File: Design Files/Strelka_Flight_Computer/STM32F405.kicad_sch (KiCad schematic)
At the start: 21 parts

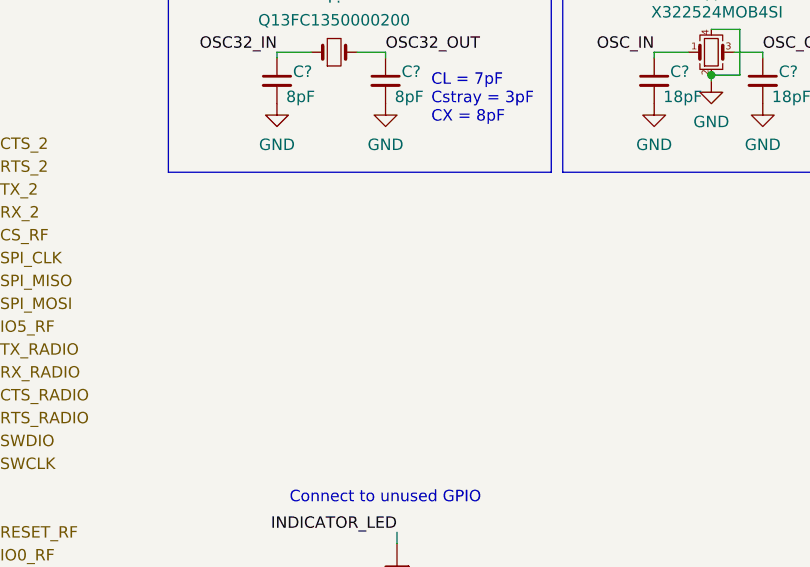
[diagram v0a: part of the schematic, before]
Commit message: Added BMX055
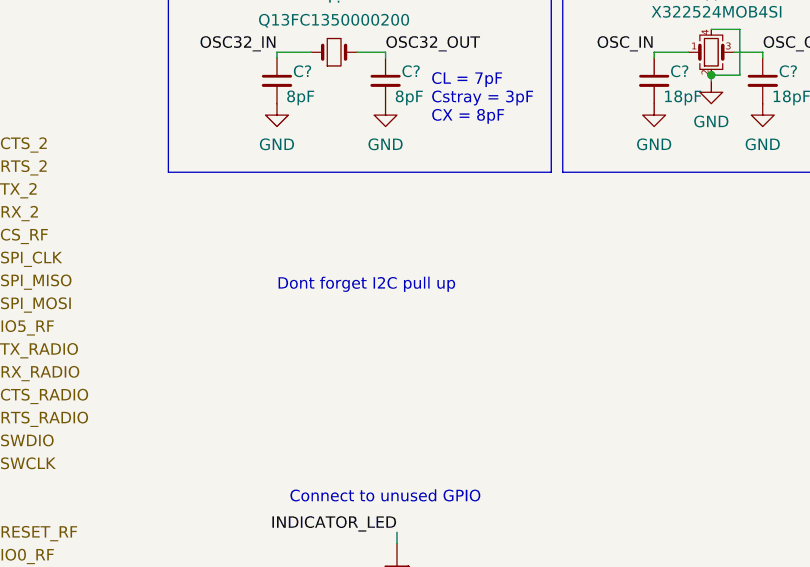
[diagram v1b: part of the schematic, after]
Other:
- note added: "Dont forget I2C pull up"
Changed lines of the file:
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@@
+    (effects (font (size 1.27 1.27)) (justify left bottom))
+  )
+  (text "Dont forget I2C pull up" (at 191.77 83.82 0)
     (effects (font (size 1.27 1.27)) (justify left bottom))
   )

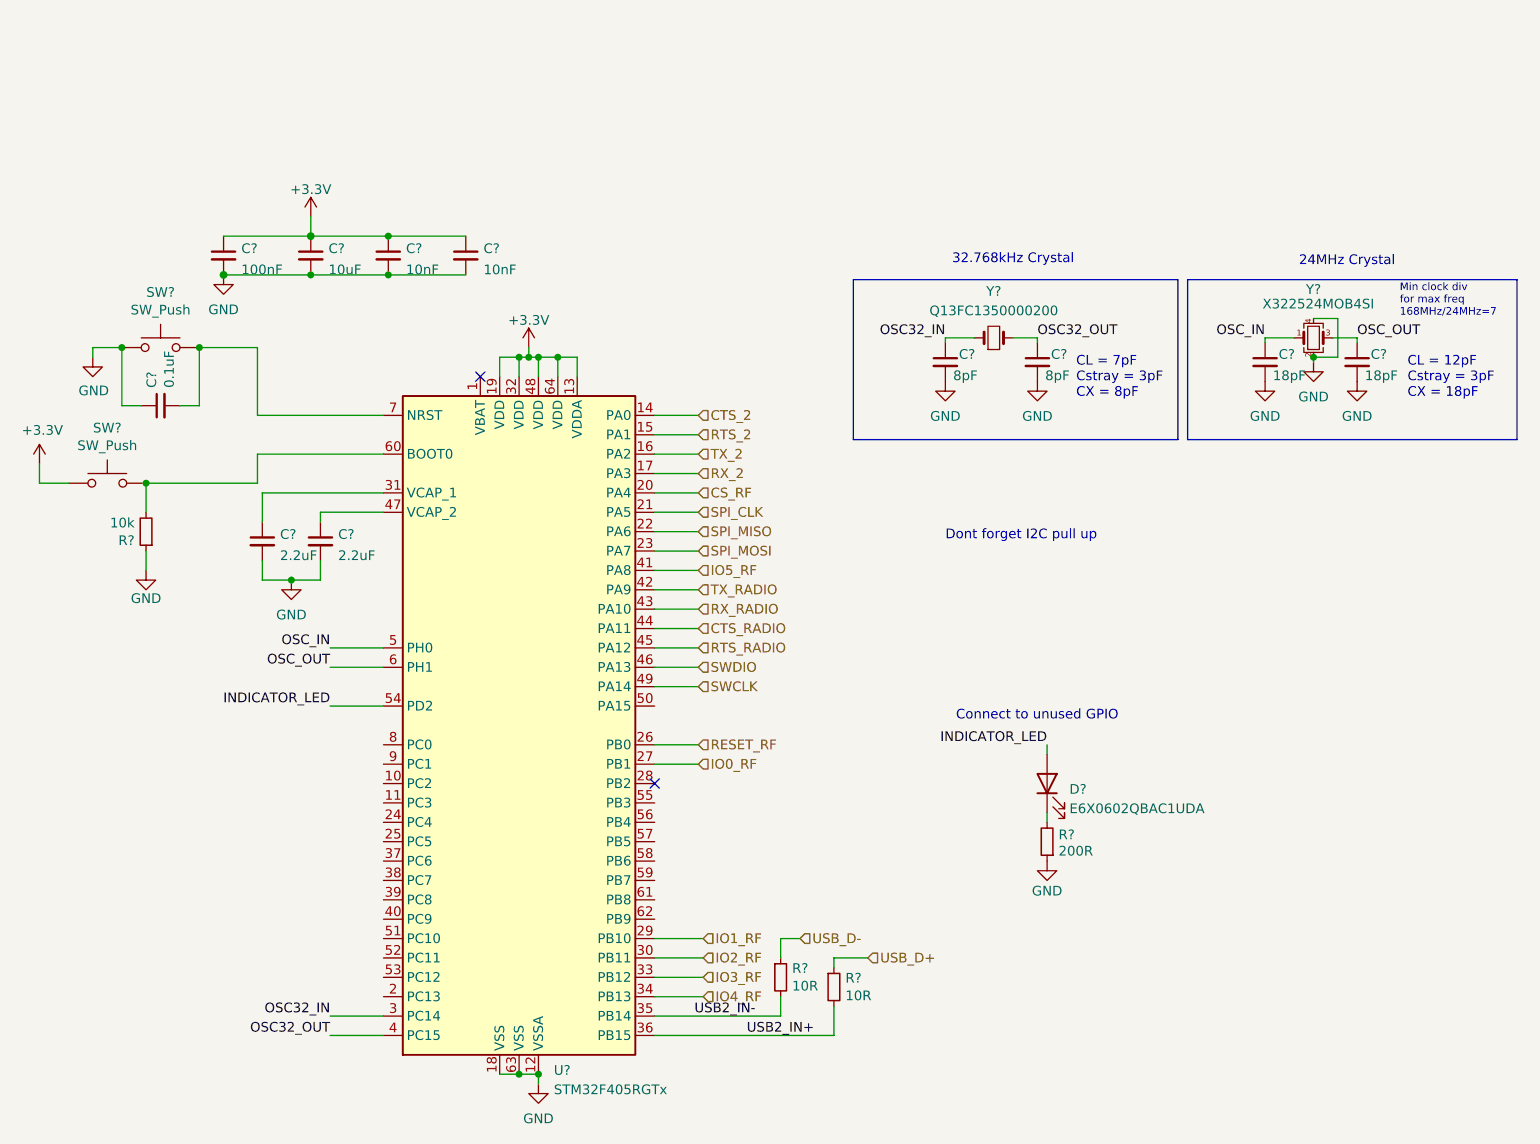
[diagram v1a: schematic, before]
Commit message: Working SPICE sim for ematch continuity circuit
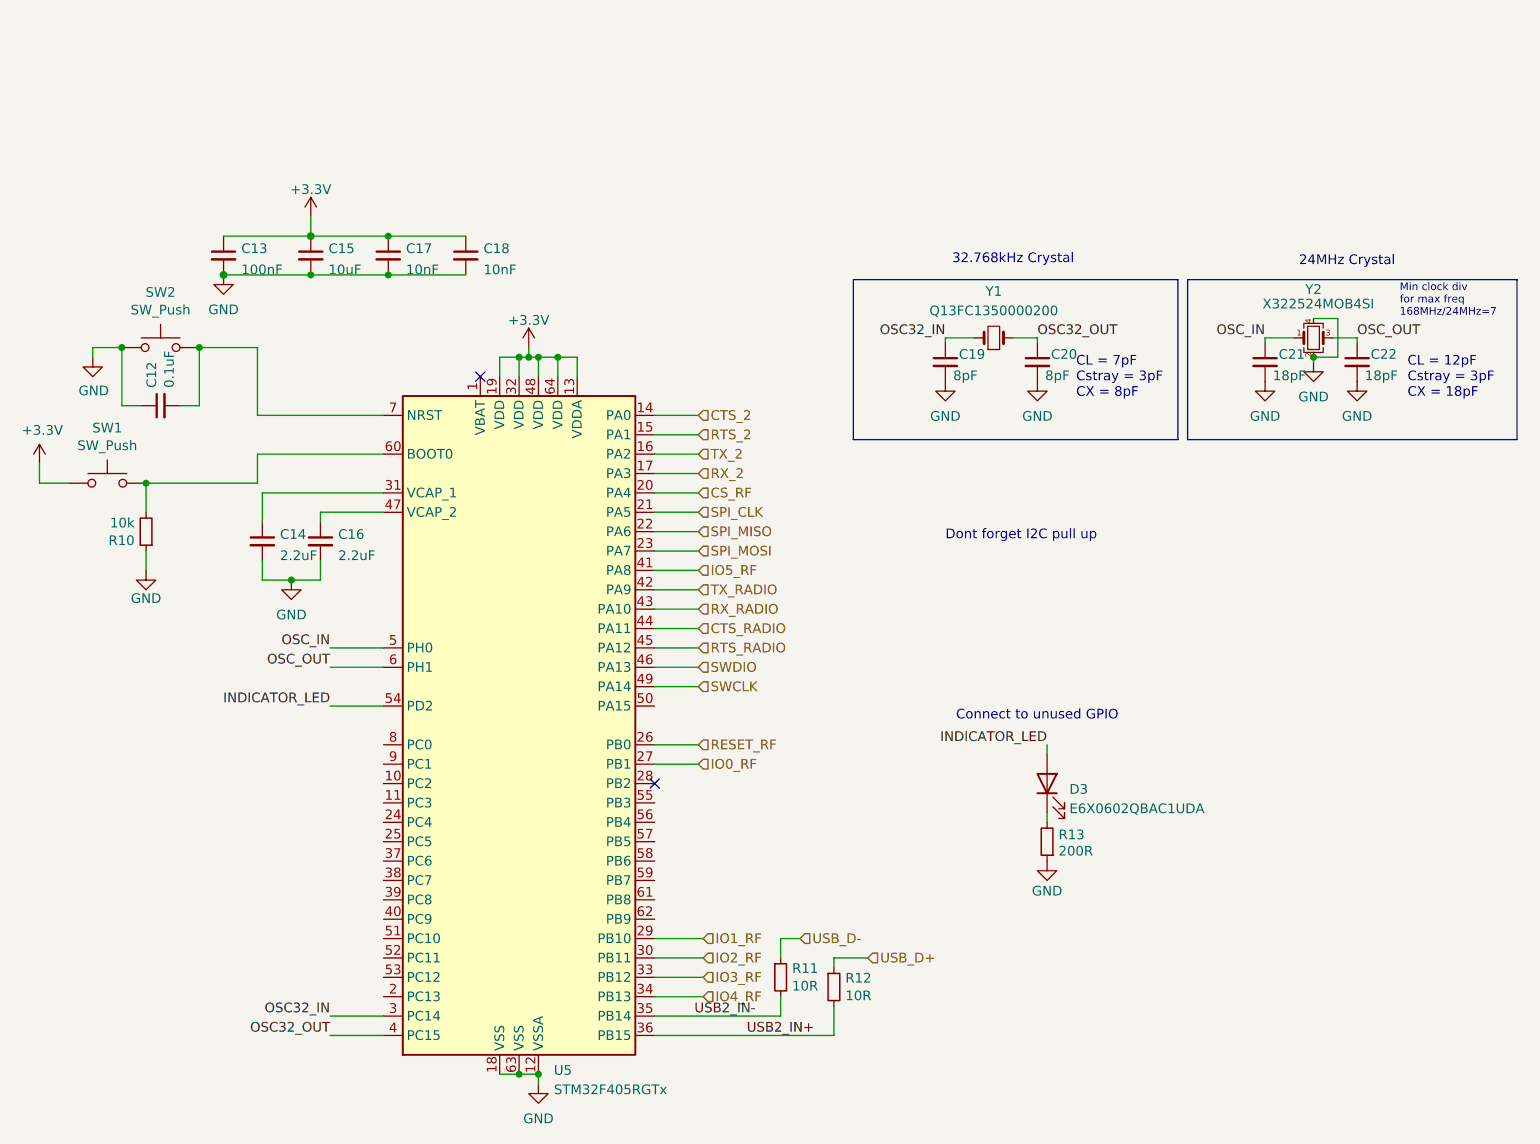
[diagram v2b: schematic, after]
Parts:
- gave numbers to parts that had none: 21

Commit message: Added power board, almost finished Strelka schematic
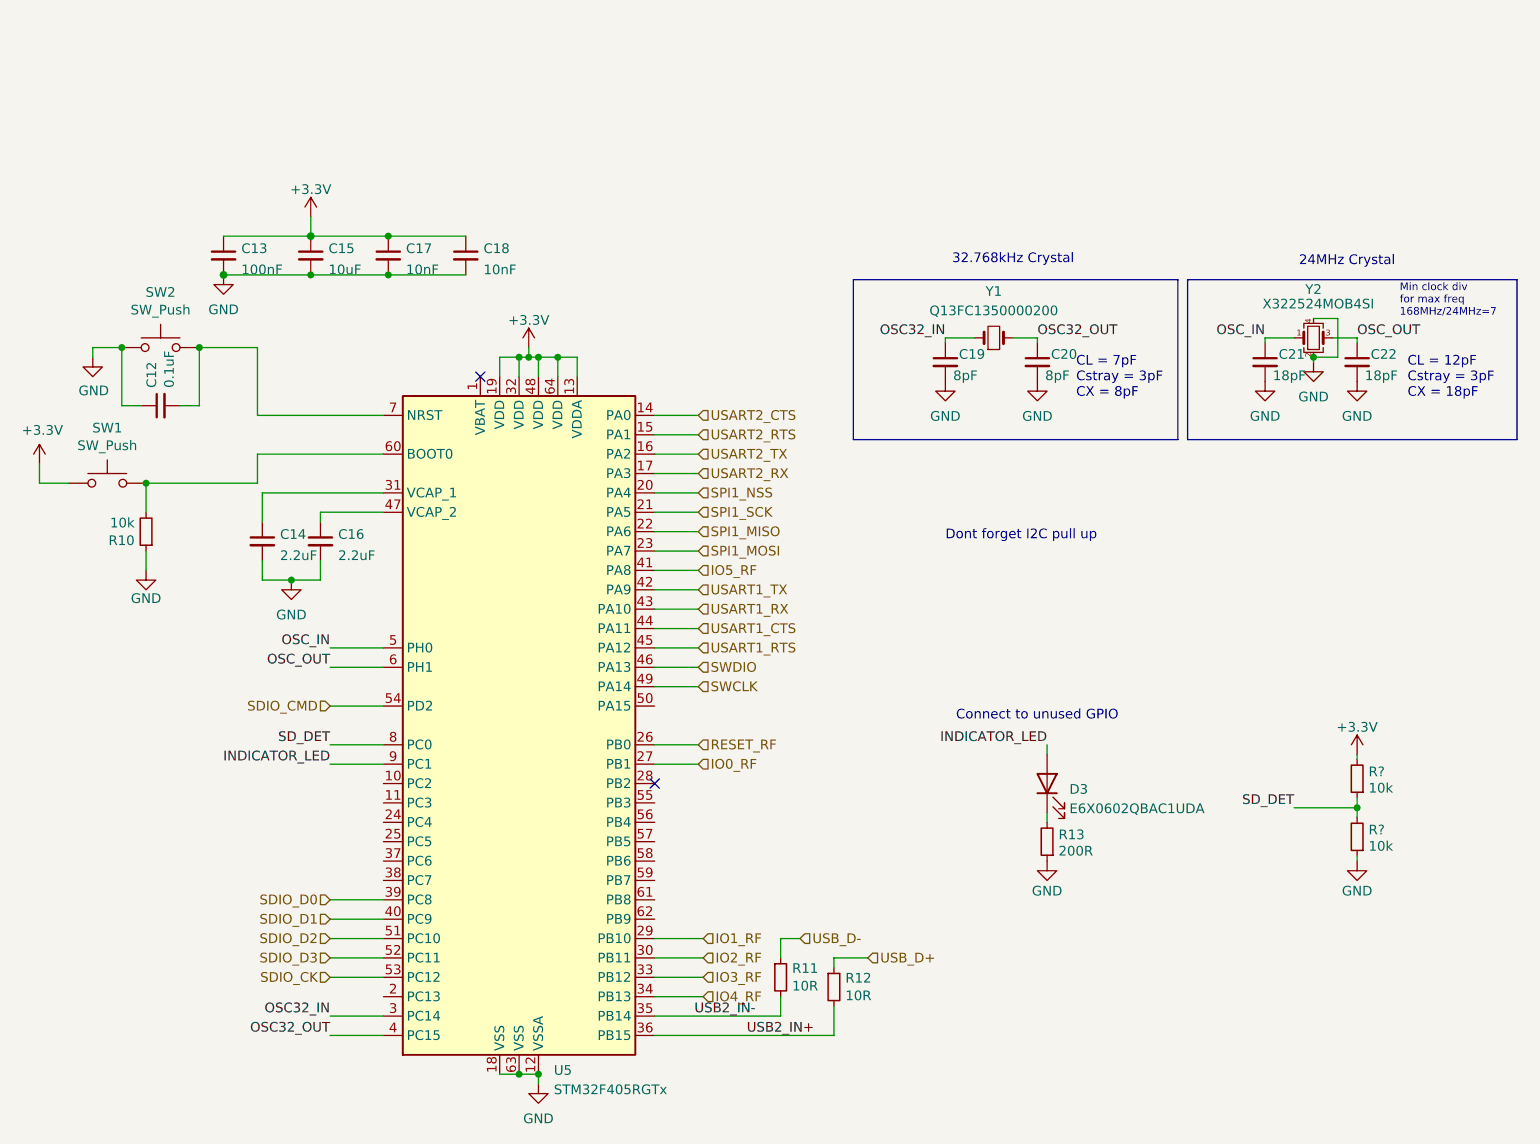
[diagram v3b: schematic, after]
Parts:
- added R? (x2): 10k, Resistor_SMD:R_0603_1608Metric_Pad0.98x0.95mm_HandSolder, symbol Device:R_Small
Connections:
- net +3V3: now also R?.2
- net GND: now also R?.1
- net INDICATOR_LED: now also U5.9 (PC1); no longer U5.54 (PD2)
- net SDIO_D0: now reaches U5.39 (PC8)
- net SDIO_D1: now reaches U5.40 (PC9)
- net SDIO_D2: now reaches U5.51 (PC10)
- net SDIO_D3: now reaches U5.52 (PC11)
- net SDIO_CK: now reaches U5.53 (PC12)
- net SD_DET: now reaches U5.8 (PC0)
- net SD_DET: now also R?.1, R?.2
- net CS_RF renamed SPI1_NSS
- net CTS_2 renamed USART2_CTS
- net CTS_RADIO renamed USART1_CTS
- net RTS_2 renamed USART2_RTS
- net RTS_RADIO renamed USART1_RTS
- net RX_2 renamed USART2_RX
- net RX_RADIO renamed USART1_RX
- net SPI_CLK renamed SPI1_SCK
- net SPI_MISO renamed SPI1_MISO
- net SPI_MOSI renamed SPI1_MOSI
- net TX_2 renamed USART2_TX
- net TX_RADIO renamed USART1_TX
- new net SDIO_CMD: U5.54 (PD2)

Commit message: Pin mapping and created STM32 .ioc for reference
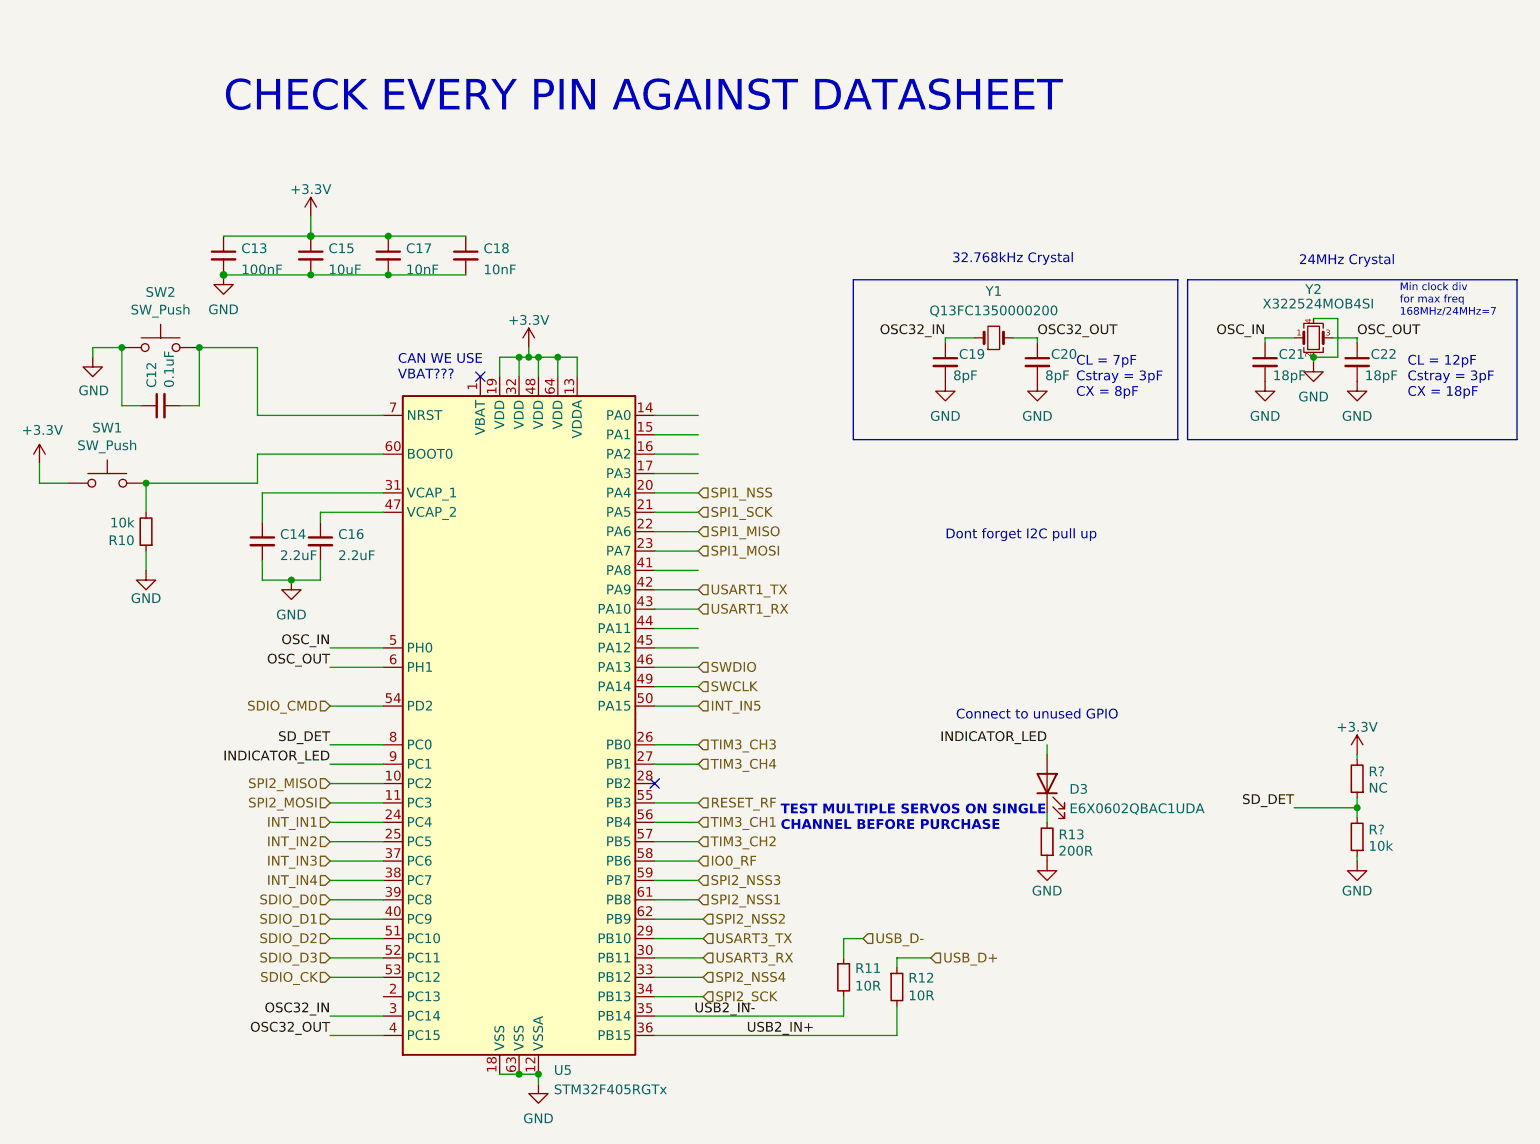
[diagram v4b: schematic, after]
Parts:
- R?: value 10k -> NC
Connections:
- net IO0_RF: now also U5.58 (PB6); no longer U5.27 (PB1)
- net RESET_RF: now also U5.55 (PB3); no longer U5.26 (PB0)
- net SPI2_MISO: now reaches U5.10 (PC2)
- net SPI2_MOSI: now reaches U5.11 (PC3)
- net INT_IN1: now reaches U5.24 (PC4)
- net INT_IN2: now reaches U5.25 (PC5)
- net INT_IN3: now reaches U5.37 (PC6)
- net INT_IN4: now reaches U5.38 (PC7)
- net INT_IN5: now reaches U5.50 (PA15)
- net TIM3_CH1: now reaches U5.56 (PB4)
- net TIM3_CH2: now reaches U5.57 (PB5)
- net SPI2_NSS3: now reaches U5.59 (PB7)
- net SPI2_NSS1: now reaches U5.61 (PB8)
- net SPI2_NSS2: now reaches U5.62 (PB9)
- net IO1_RF renamed USART3_TX
- net IO2_RF renamed USART3_RX
- net IO3_RF renamed SPI2_NSS4
- net IO4_RF renamed SPI2_SCK
- net IO5_RF: no longer names the net of U5.41 (PA8)
- net USART1_CTS: no longer names the net of U5.44 (PA11)
- net USART1_RTS: no longer names the net of U5.45 (PA12)
- net USART2_CTS: no longer names the net of U5.14 (PA0)
- net USART2_RTS: no longer names the net of U5.15 (PA1)
- net USART2_RX: no longer names the net of U5.17 (PA3)
- net USART2_TX: no longer names the net of U5.16 (PA2)
- new net TIM3_CH3: U5.26 (PB0)
- new net TIM3_CH4: U5.27 (PB1)
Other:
- note added: "CAN WE USE VBAT???"
- note added: "CHECK EVERY PIN AGAINST DATASHEET"
- note added: "TEST MULTIPLE SERVOS ON SINGLE CHANNEL BEFORE PURCHASE"
- moved on the sheet: R11, R12
